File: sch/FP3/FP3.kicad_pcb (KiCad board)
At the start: 2 copper layers, 32 x 40 mm, 11 parts, among them J1 module_connector_header, J2 MXDOT_Prog_Header_Keyed, U1 MTXDOT-EU1-A00-100

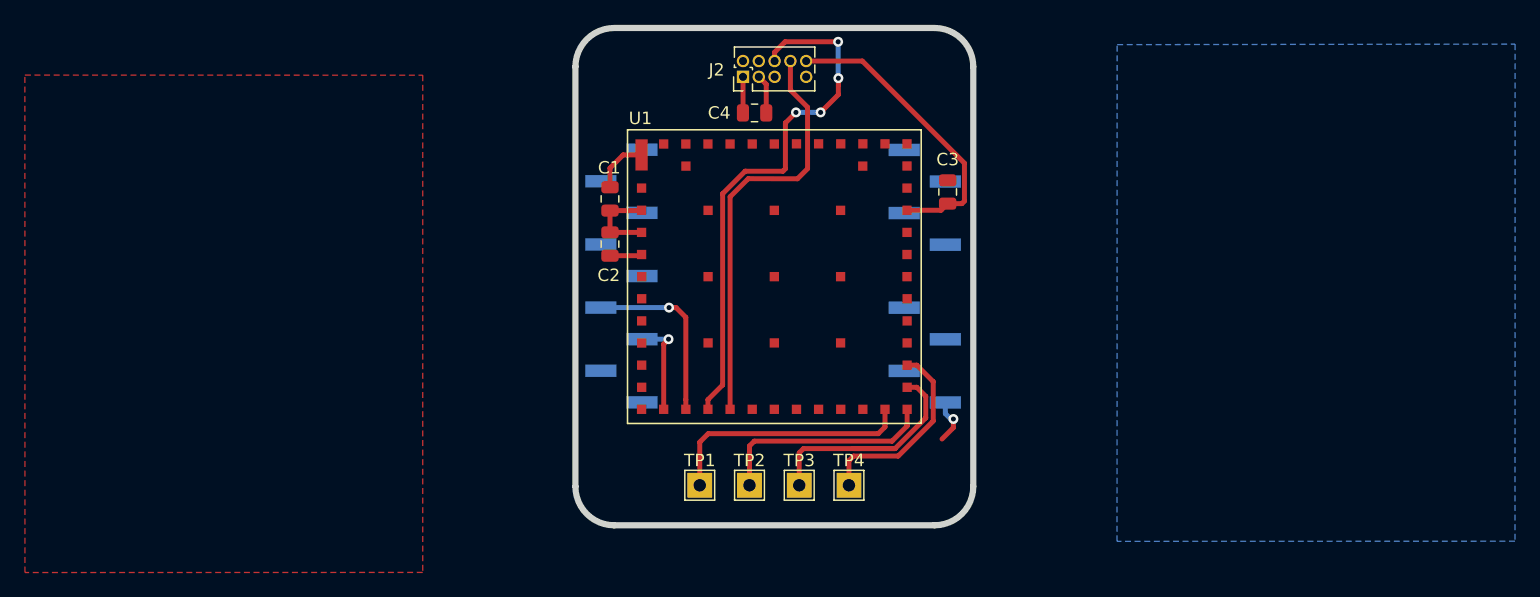
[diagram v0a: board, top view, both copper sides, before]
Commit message: Finished FP3 sch and PCB, updated title blocks.
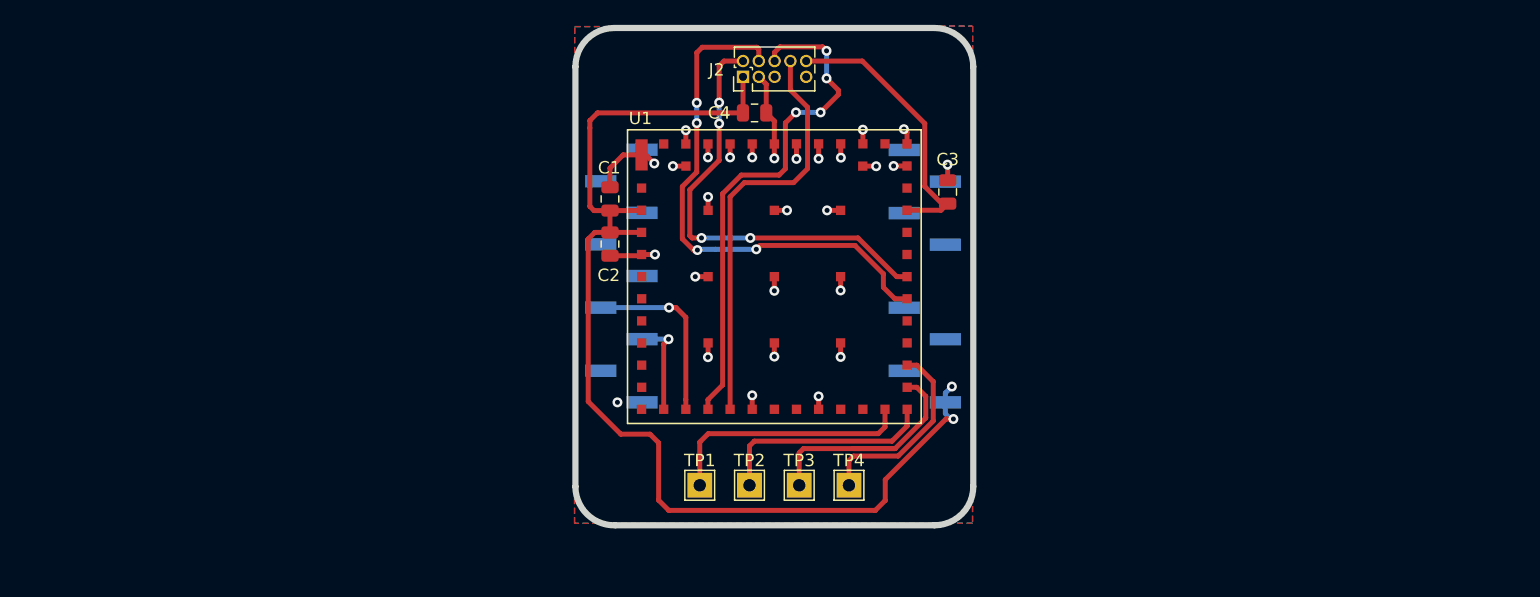
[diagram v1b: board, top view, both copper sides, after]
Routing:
- net +3V3: track 13.5 -> 89.0 mm, vias 1 -> 2
- net /SWCLK: track 0.00 -> 42.7 mm, vias 0 -> 4
- net /SWDIO: track 0.00 -> 35.6 mm, vias 0 -> 4
- net GND: track 10.2 -> 43.4 mm, vias 0 -> 28
- net /NRESET: track 24.1 -> 22.6 mm
- net /MBED_RX: track 43.2 -> 41.9 mm
- added copper zone on F.Cu, net +3V3
- removed copper zone on F.Cu, net GND
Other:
- outline, holes or cut-outs redrawn

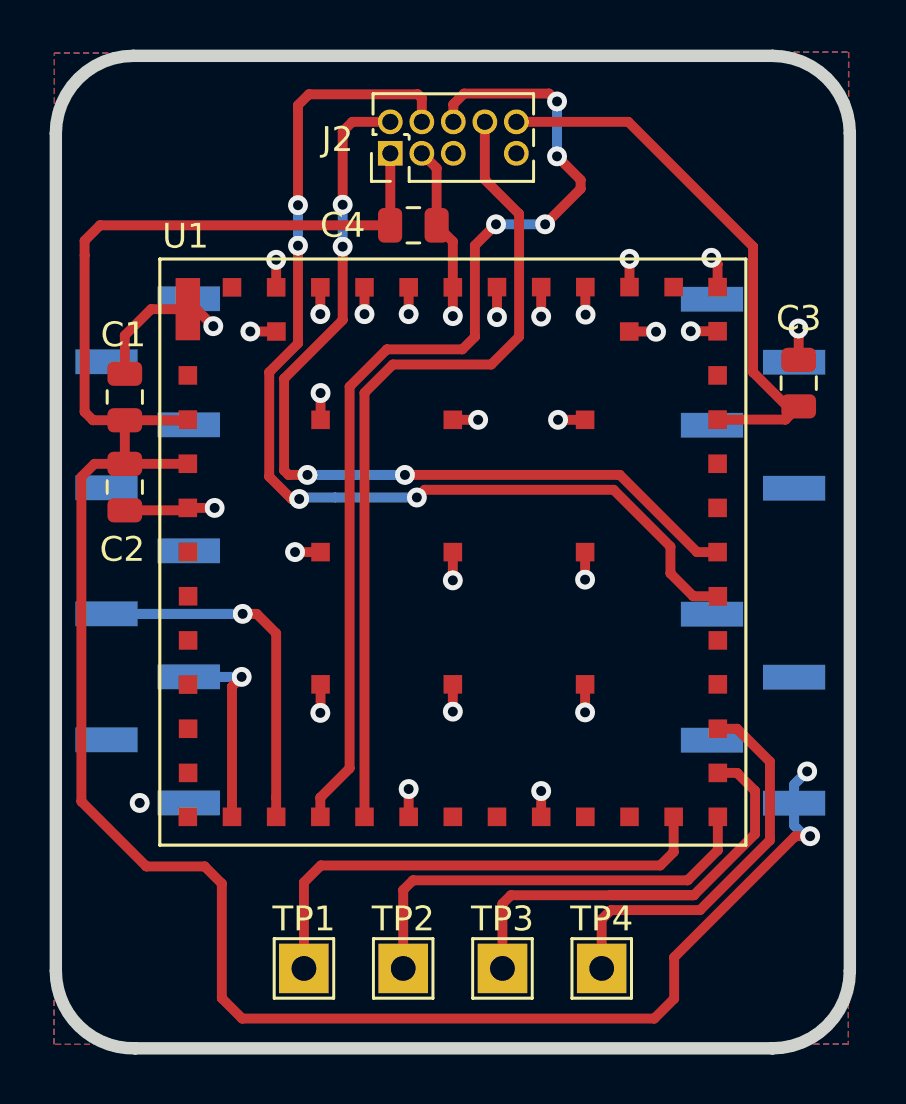
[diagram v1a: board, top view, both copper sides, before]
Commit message: Added test points and connector details for FP3.
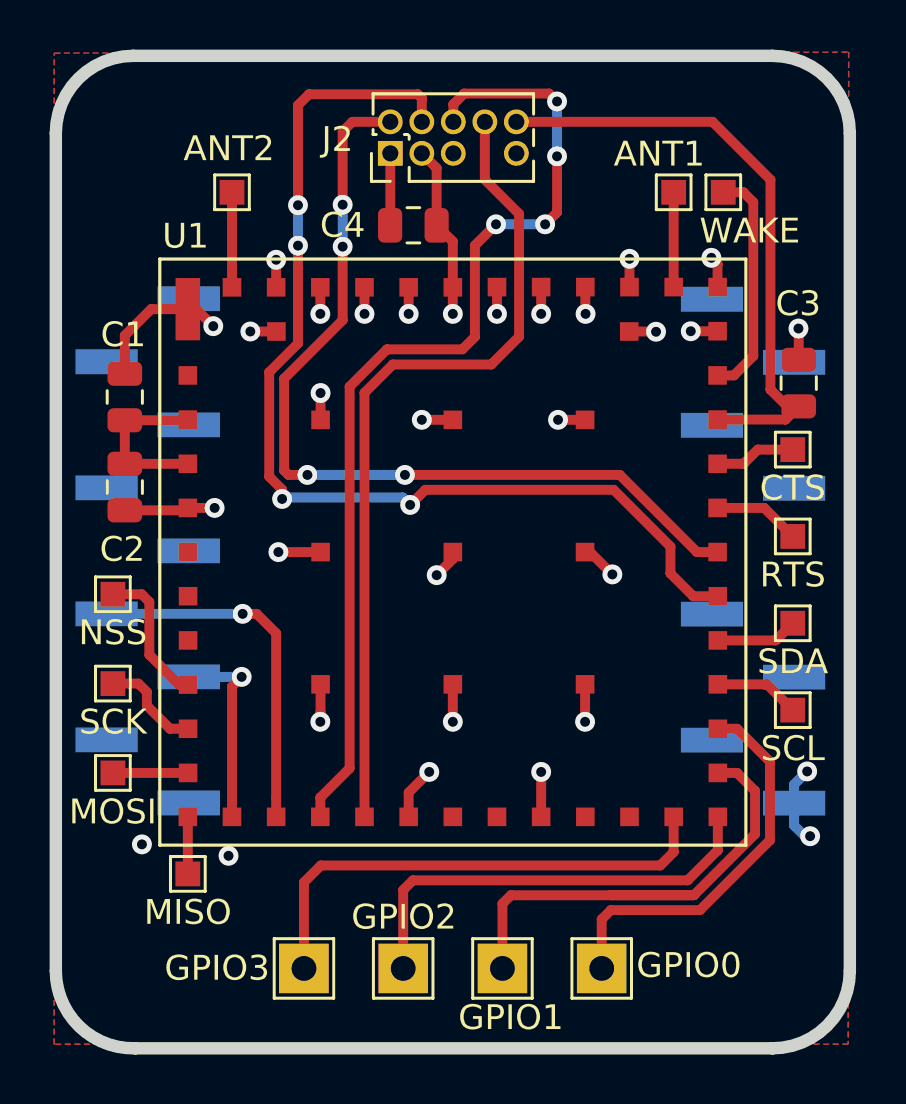
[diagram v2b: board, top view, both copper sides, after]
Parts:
- added G1: Logo-NewieVentures-75px, newie:logo_14.2x12.1mm, B.Cu at (145.4, 97.2)
- added TP10: MISO, TestPoint:TestPoint_Pad_1.0x1.0mm, F.Cu at (134.3, 113.0)
- added TP11: RTS, TestPoint:TestPoint_Pad_1.0x1.0mm, F.Cu at (158.7, 99.4)
- added TP12: SCL, TestPoint:TestPoint_Pad_1.0x1.0mm, F.Cu at (158.7, 106.4)
- added TP13: SDA, TestPoint:TestPoint_Pad_1.0x1.0mm, F.Cu at (158.7, 102.9)
- added TP14: ANT1, TestPoint:TestPoint_Pad_1.0x1.0mm, F.Cu at (153.9, 85.5)
- added TP15: ANT2, TestPoint:TestPoint_Pad_1.0x1.0mm, F.Cu at (136.1, 85.5)
- added TP5: WAKE, TestPoint:TestPoint_Pad_1.0x1.0mm, F.Cu at (155.9, 85.5)
- added TP6: NSS, TestPoint:TestPoint_Pad_1.0x1.0mm, F.Cu at (131.3, 101.7)
- added TP7: SCK, TestPoint:TestPoint_Pad_1.0x1.0mm, F.Cu at (131.3, 105.3)
- added TP8: MOSI, TestPoint:TestPoint_Pad_1.0x1.0mm, F.Cu at (131.3, 108.9)
- added TP9: CTS, TestPoint:TestPoint_Pad_1.0x1.0mm, F.Cu at (158.7, 95.9)
- U1: value MTXDOT-EU1-A00-100 -> MTXDOT-AU1-A01-100
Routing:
- net +3V3: track 89.0 -> 13.0 mm
- net Net-(TP5-Pad1): track 0.00 -> 9.34 mm
- net Net-(TP6-Pad1): track 0.00 -> 5.79 mm
- net Net-(TP7-Pad1): track 0.00 -> 4.11 mm
- net Net-(TP15-Pad1): track 0.00 -> 3.83 mm
- net Net-(TP14-Pad1): track 0.00 -> 3.82 mm
- net Net-(TP11-Pad1): track 0.00 -> 3.51 mm
- net Net-(TP12-Pad1): track 0.00 -> 3.45 mm
- net GND: track 43.4 -> 46.7 mm, vias 28 -> 29
- net Net-(TP13-Pad1): track 0.00 -> 3.31 mm
- net Net-(TP9-Pad1): track 0.00 -> 3.27 mm
- net Net-(TP8-Pad1): track 0.00 -> 3.03 mm
- net Net-(TP10-Pad1): track 0.00 -> 2.30 mm
- net /NRESET: track 22.6 -> 24.6 mm
- net /MBED_RX: track 41.9 -> 41.1 mm
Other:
- board text added: "FP3 rev A 2019-07-16"
